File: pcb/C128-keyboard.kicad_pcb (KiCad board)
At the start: 2 copper layers, 395.1 x 132 mm, 104 parts, among them CN2 C128, SW1 Inst/Del, SW10 Esc, SW11 Alt, SW12 Return, SW13 W, SW14 R, SW15 Y, SW16 I, SW17 P, SW18 *, SW19 LeftArrow, SW2 3, SW20 Num8, SW21 Num+, SW22 Num0, SW23 Crsr Horiz, SW24 A, SW25 D, SW26 G, SW27 J, SW28 L, SW29 ;, SW3 5, SW30 Ctrl, SW31 Num5, SW32 Num-, SW33 Num., SW34 F7, SW35 4, SW36 6, SW37 8, SW38 0, SW39 -, SW4 7, SW40 Clr/Home, SW41 2, SW42 Tab, SW43 LineFeed, SW44 Crsr-Up, SW45 F1, SW46 Z, SW47 C, SW48 B, SW49 M, SW5 9, SW50 ., SW51 R-Shift, SW52 Space, SW53 Num2, SW54 NumEnter, SW55 Crsr-Down, SW56 F3, SW57 S, SW58 F, SW59 H, SW6 +, SW60 K, SW61 :, SW62 =, SW63 C=, SW64 Num4, SW65 Num6, SW66 Crsr-Left, SW67 F5, SW68 E, SW69 T, SW7 £, SW70 U, SW71 O, SW72 @, SW73 UpArrow, SW74 Q, SW75 Num7, SW76 Num9, SW77 Crsr-Right, SW78 Crsr Vert, SW79 L-Shift, SW8 1, SW80 X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

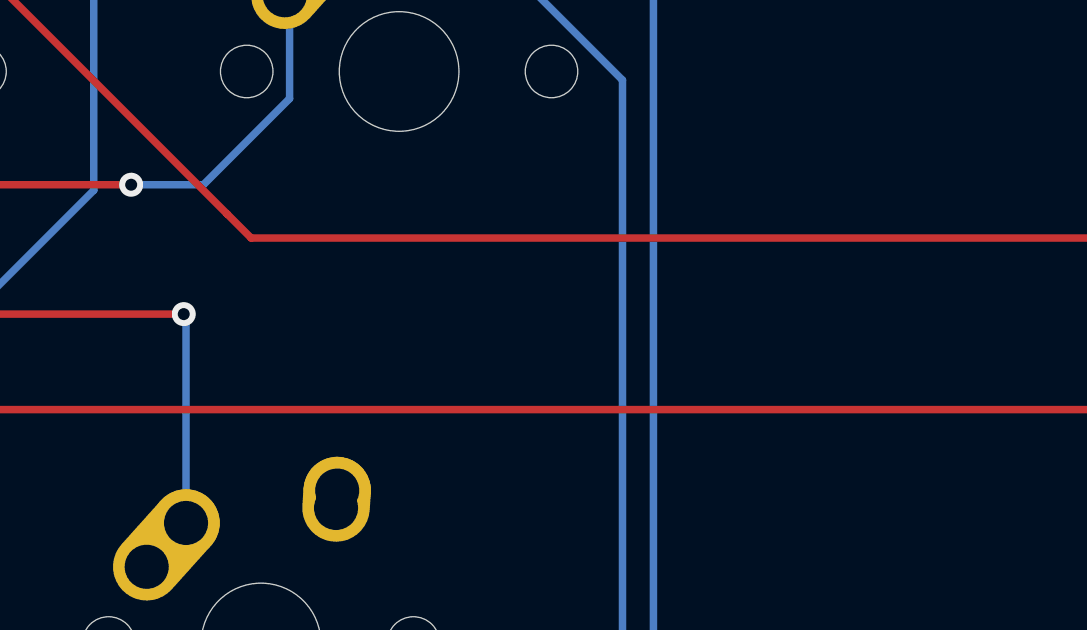
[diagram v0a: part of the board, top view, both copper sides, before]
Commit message: PCB 2.2 with extra restore pin
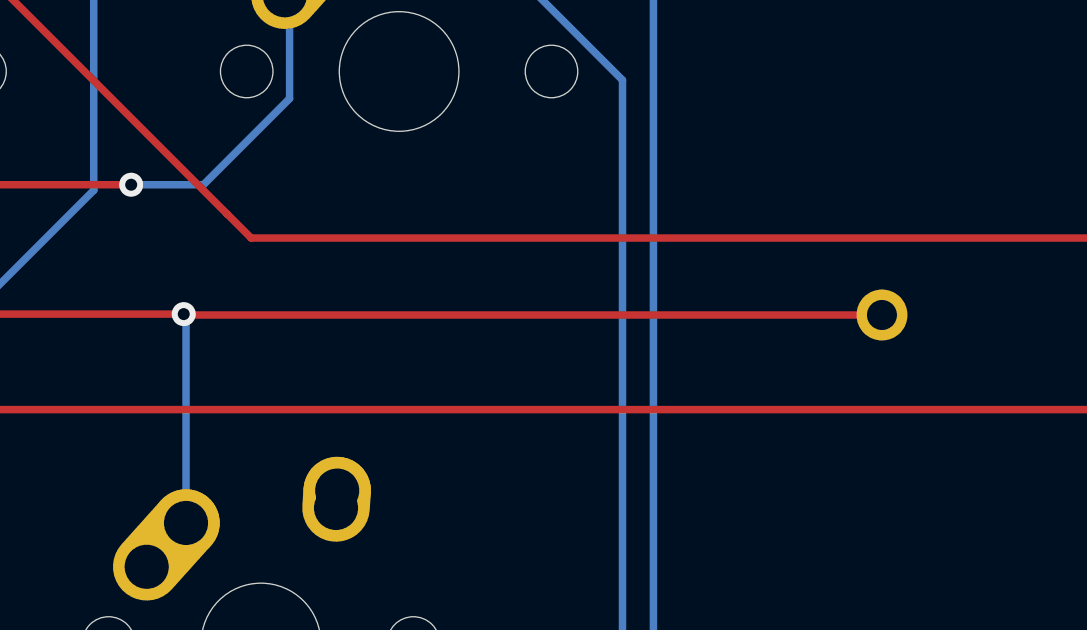
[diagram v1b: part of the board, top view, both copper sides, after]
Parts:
- added ?: , , F.Cu at (420.1, 127.8)
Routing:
- net Restore: track 112.3 -> 135.7 mm
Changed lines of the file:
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@@
 	(paper "A2")
 	(title_block
-		(date "2025-10-13")
-		(rev "rev.2.1")
+		(date "2025-10-18")
+		(rev "rev.2.2")
 	)
 	(layers
@@
 		(embedded_fonts no)
 	)
+	(footprint ""
+		(layer "F.Cu")
+		(at 420.1 127.85)
+		(property "Reference" ""
+			(at 0 0 0)
+			(layer "F.SilkS")
+			(effects
+				(font
+					(size 1.27 1.27)
+					(thickness 0.15)
+				)
+			)
+		)
+		(property "Value" ""
+			(at 0 0 0)
+			(layer "F.Fab")
+			(effects
+				(font
+					(size 1.27 1.27)
+					(thickness 0.15)
+				)
+			)
+		)
+		(property "Datasheet" ""
+			(at 0 0 0)
+			(layer "F.Fab")
+			(hide yes)
+			(effects
+				(font
+					(size 1.27 1.27)
+					(thickness 0.15)
+				)
+			)
+		)
+		(property "Description" ""
+			(at 0 0 0)
+			(layer "F.Fab")
+			(hide yes)
+			(effects
+				(font
+					(size 1.27 1.27)
+					(thickness 0.15)
+				)
+			)
+		)
+		(pad "16" thru_hole oval
+			(at 0 0 270)
+			(size 1.7 1.7)
+			(drill 1)
+			(layers "*.Cu" "*.Mask")
+			(remove_unused_layers no)
+			(net 2 "Restore")
+			(pinfunction "Pin_16")
+			(pintype "passive")
+		)
+		(embedded_fonts no)
+	)
 	(footprint "MX_Alps_Hybrid:MX-1U-NoLED"
 		(layer "F.Cu")
@@
 		)
 	)
+	(gr_text "RSTO"
+		(at 427.1 128.725 0)
+		(layer "B.SilkS")
+		(effects
+			(font
+				(size 1.5 1.5)
+				(thickness 0.3)
+				(bold yes)
+			)
+			(justify left bottom mirror)
+		)
+	)
 	(gr_text "COL7"
 		(at 349.775 106.4 90)
@@
 	)
 	(segment
+		(start 396.855764 127.85)
+		(end 396.826014 127.82025)
+		(width 0.25)
+		(layer "F.Cu")
+		(net 2)
+	)
+	(segment
+		(start 420.1 127.85)
+		(end 396.855764 127.85)
+		(width 0.25)
+		(layer "F.Cu")
+		(net 2)
+	)
+	(segment
 		(start 396.826014 127.82025)
 		(end 317.044764 127.82025)
 		(width 0.25)
 		(layer "F.Cu")
+		(net 2)
+	)
+	(segment
+		(start 420.4 127.9)
+		(end 420.32025 127.82025)
+		(width 0.25)
+		(layer "F.Cu")

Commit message: Edge cut cleanup
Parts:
- removed Plate Ground: MountingHole_3.2mm_M3_Pad_Via, MountingHole:MountingHole_3.2mm_M3_Pad_Via
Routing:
- net 40_80: track 85.5 -> 74.7 mm
- net CAPLK: track 203.0 -> 193.1 mm
- net COL10: track 450.5 -> 446.4 mm
- net COL8: track 457.7 -> 455.9 mm
- net COL9: track 532.3 -> 531.3 mm
- net GND: vias 151 -> 152
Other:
- board size 395.1 x 132 mm -> 395.2 x 125.9 mm
- board text removed: "Plate Ground"
